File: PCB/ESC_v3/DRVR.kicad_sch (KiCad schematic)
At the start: 15 parts, among them U2 DRV8323SRTAT

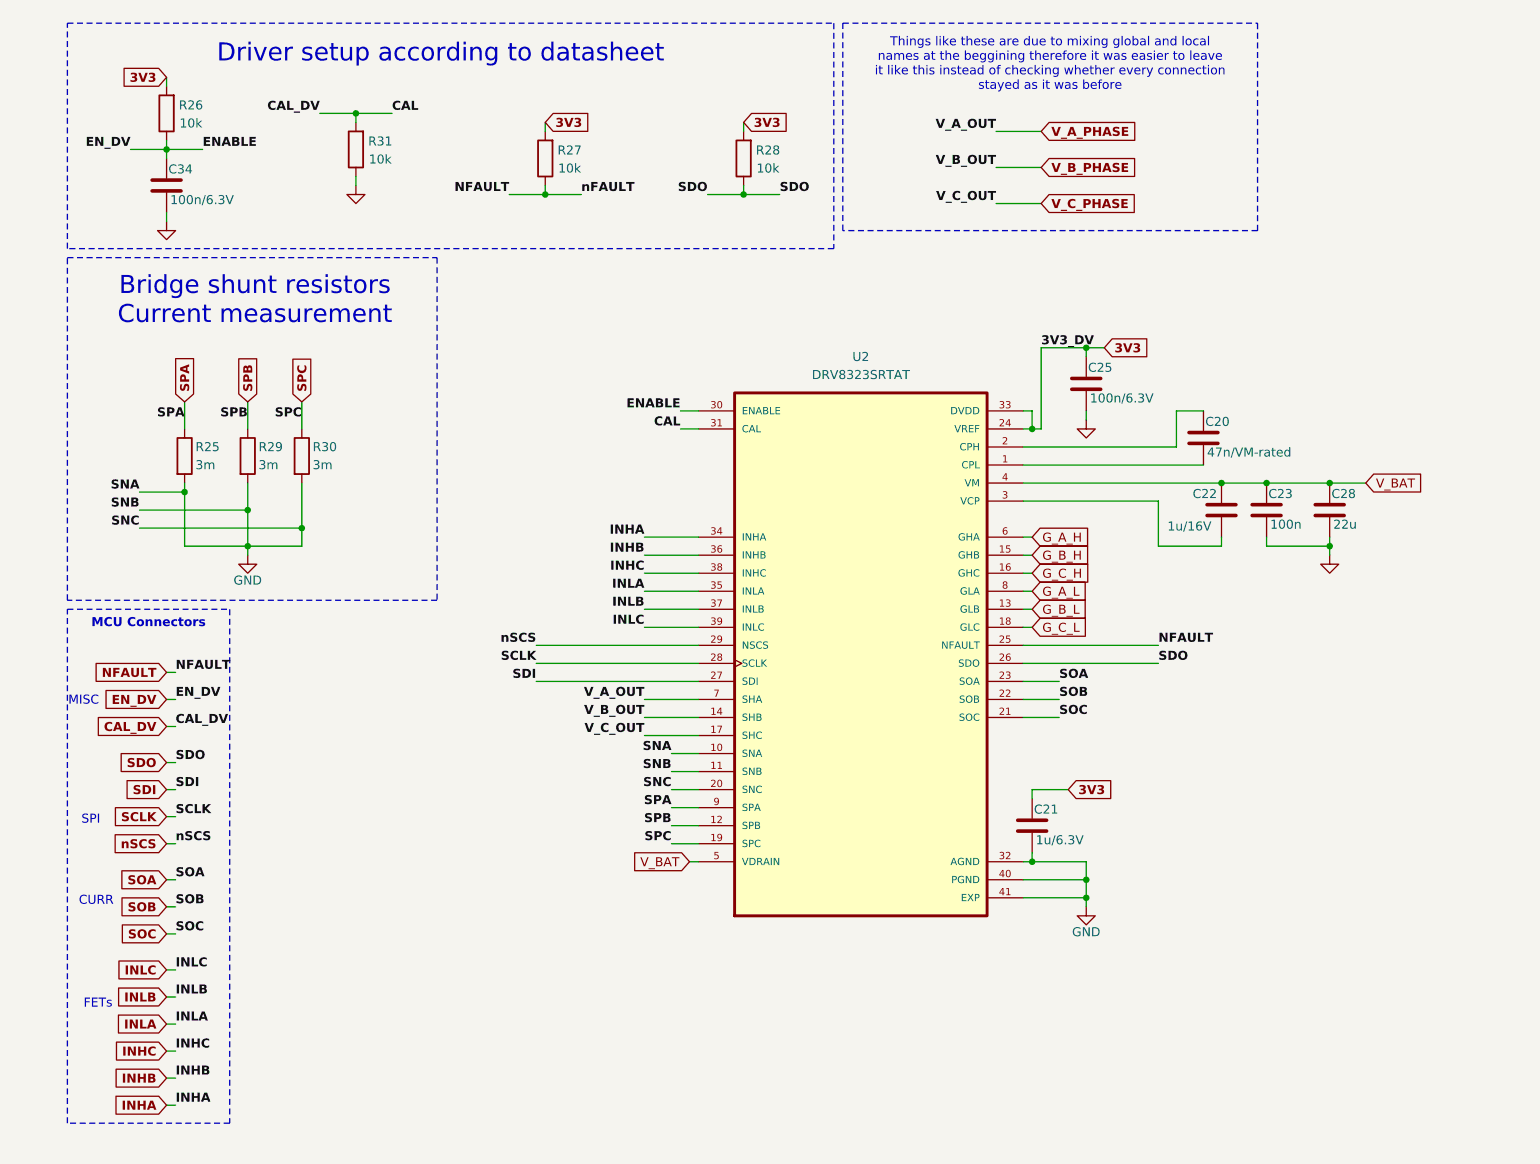
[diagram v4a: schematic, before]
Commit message: Update ESC_v3 schematics and PCB layout
Add net-tie symbol and +3V3/GND1 power symbols to DRVR schematic and reorganize schematic graphics (rectangles, text), junctions, and wires with updated coordinates/UUIDs. Also update top-level ESC_v3 schematic and MCU schematic along with PCB (.kicad_pcb) and panel (.kicad_prl) files. Remove several old backup zip files and add new backups for the ESC_v3 project.
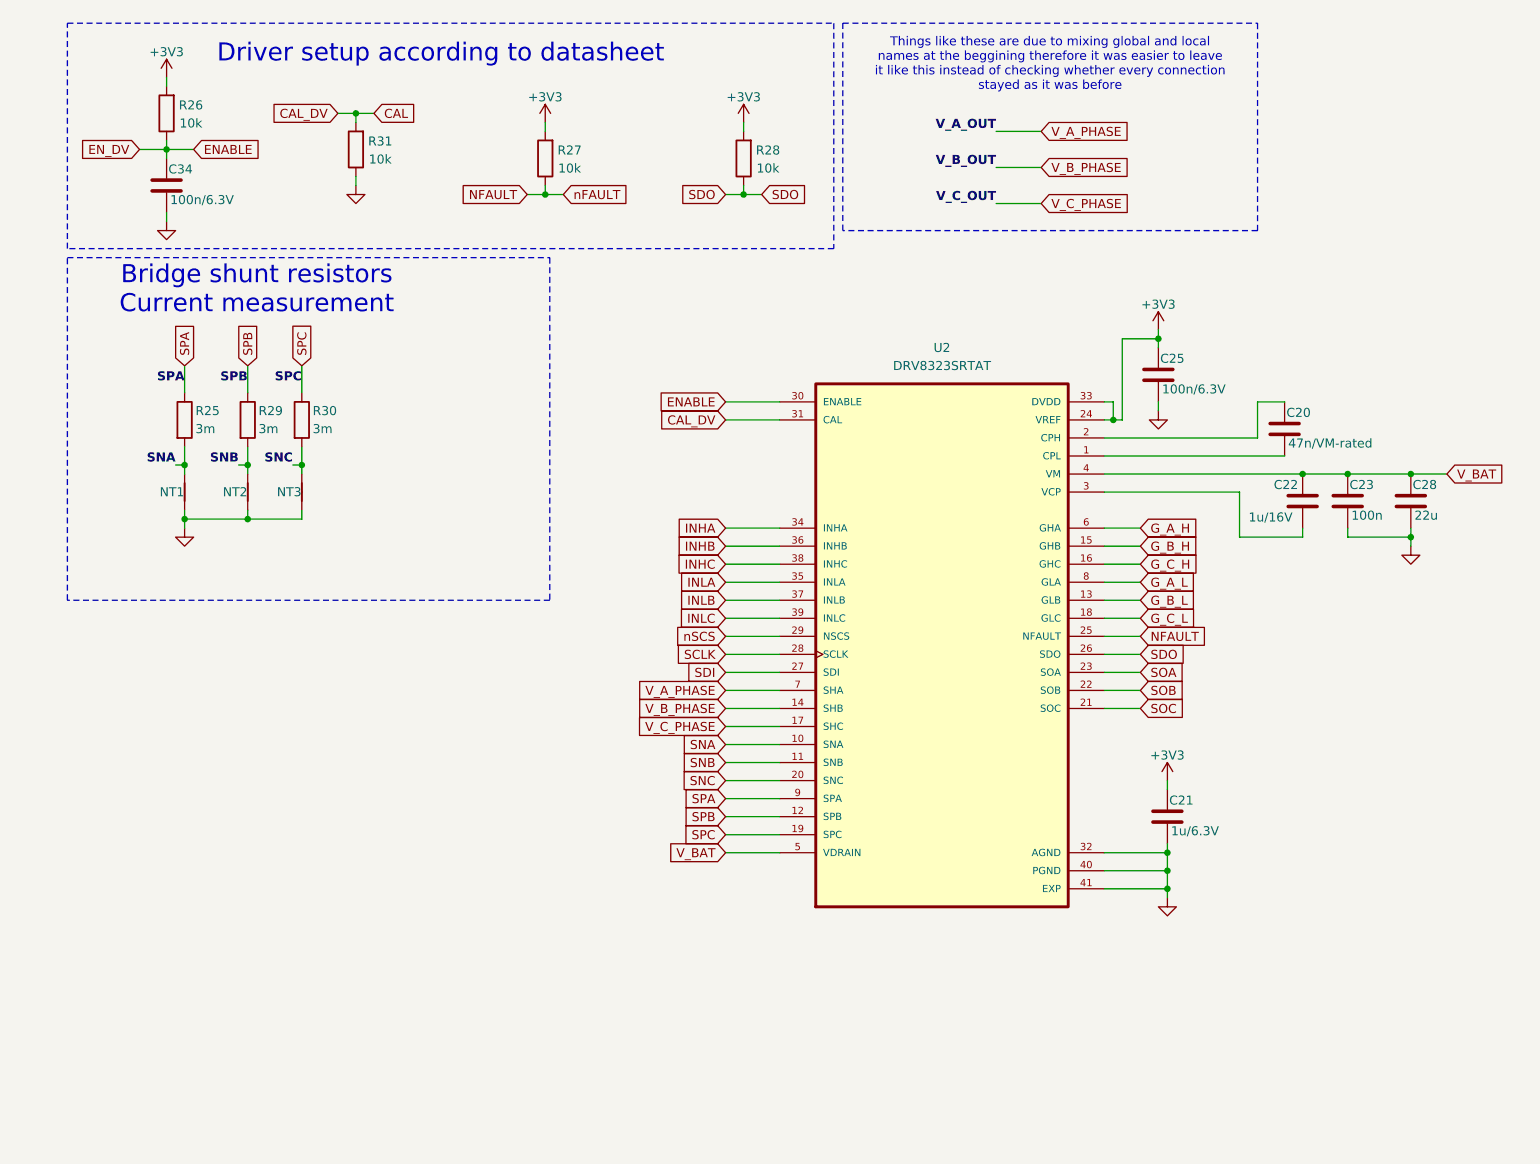
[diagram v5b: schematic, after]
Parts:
- added NT1, NT2, NT3: NetTie_2, symbol Device:NetTie_2
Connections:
- net GND: now also NT1.1, NT2.1, NT3.1; no longer R25.2, R29.2, R30.2, U2.10 (SNA), U2.11 (SNB), U2.20 (SNC)
- net 3V3 renamed +3V3
- net CAL_DV renamed CAL
- net EN_DV renamed ENABLE
- new net SNA: NT1.2, R25.2, U2.10 (SNA)
- new net SNB: NT2.2, R29.2, U2.11 (SNB)
- new net SNC: NT3.2, R30.2, U2.20 (SNC)
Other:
- note removed: "CURR"
- note removed: "FETs"
- note removed: "MCU Connectors"
- note removed: "MISC"
- note removed: "SPI"
- moved on the sheet: C20, C21, C22, C23, C25, C28, R25, R29, R30, U2

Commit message: Update DRVR schematic: relabels, wiring, net-ties
Refactor PCB/ESC_v3/DRVR.kicad_sch: cleaned up stray rectangles and comment text, repositioned many junctions and wires to fix connectivity, replaced/added global labels (reorganized SNA/SPA/SPB/SPC/SNB/SNC/etc.), and inserted NetTie symbols (NT1/NT3) with footprints to implement net ties. Updated symbol positions and UUIDs and removed obsolete schematic elements. Also touched top-level ESC_v3 files (ESC_v3.kicad_pcb, ESC_v3.kicad_prl, ESC_v3.kicad_sch, MCU.kicad_sch) and added/removed several backup archives.
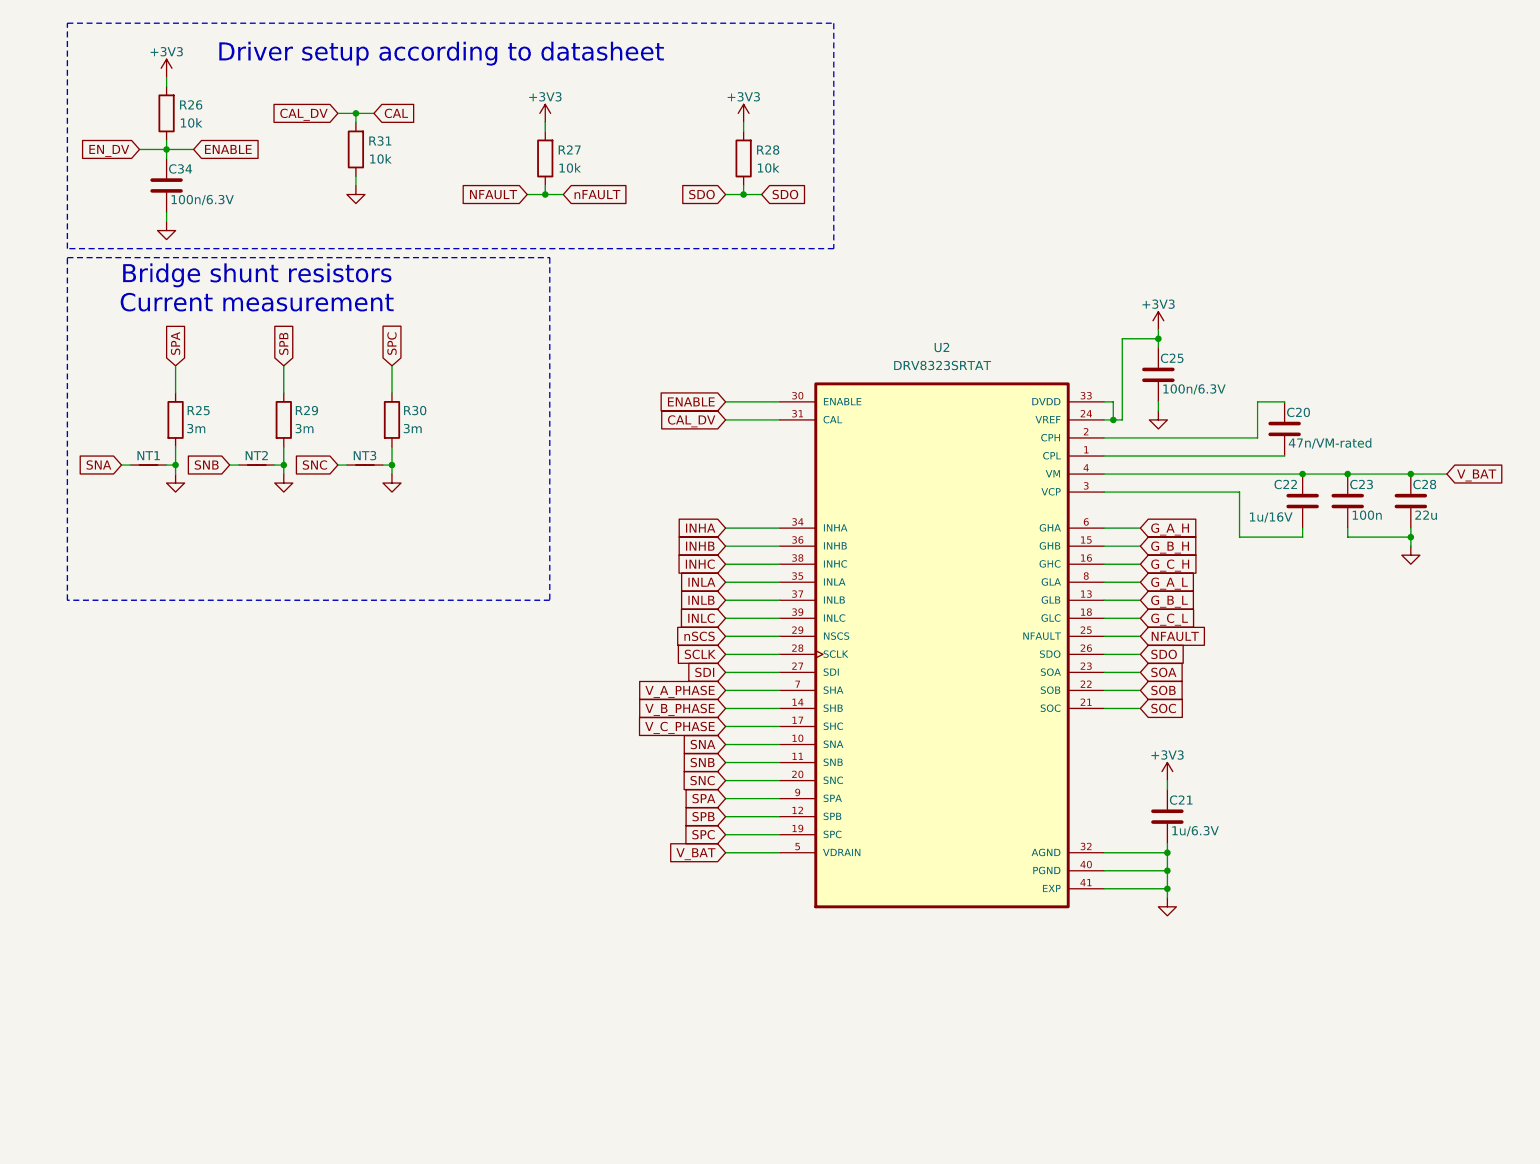
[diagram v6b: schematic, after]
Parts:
- NT1, NT2, NT3: footprint (none) -> NetTie:NetTie-2_SMD_Pad0.5mm
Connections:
- net GND: now also NT1.2, NT2.2, NT3.2, R25.2, R29.2, R30.2; no longer NT1.1, NT2.1, NT3.1
- net SNA: now also NT1.1; no longer NT1.2, R25.2
- net SNB: now also NT2.1; no longer NT2.2, R29.2
- net SNC: now also NT3.1; no longer NT3.2, R30.2
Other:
- note removed: "Things like these are due to mixing global and local names at the beggining therefore it was easier to leave it like this instead of checking whether every connection stayed as it was before"
- moved on the sheet: R25, R29, R30

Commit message: ESC_v3: footprint, PCB teardrops & backup updates
Remove Notes.txt; update ESC_v3 PCB and schematic files. In DRVR.kicad_sch several capacitor footprints changed from 0805 to 0603. ESC_v3.kicad_pcb: set grid_origin, added teardrops to multiple pads, updated many component UUIDs and silkscreen font thicknesses, and other layout metadata tweaks. Clean up old ESC_v3 backup zips and add new timestamped backup archives. Also update related KiCad project files (.kicad_prl, .kicad_pro). These changes shrink component footprints, improve manufacturability (teardrops), and refresh project backups/metadata.
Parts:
- C20, C22, C23: footprint Capacitor_SMD:C_0805_2012Metric -> Capacitor_SMD:C_0603_1608Metric
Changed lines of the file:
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@@
 			)
 		)
-		(property "Footprint" "Capacitor_SMD:C_0805_2012Metric"
+		(property "Footprint" "Capacitor_SMD:C_0603_1608Metric"
 			(at 191.4652 78.74 0)
 			(effects
@@
 			)
 		)
-		(property "Footprint" "Capacitor_SMD:C_0805_2012Metric"
+		(property "Footprint" "Capacitor_SMD:C_0603_1608Metric"
 			(at 200.3552 88.9 0)
 			(effects
@@
 			)
 		)
-		(property "Footprint" "Capacitor_SMD:C_0805_2012Metric"
+		(property "Footprint" "Capacitor_SMD:C_0603_1608Metric"
 			(at 194.0052 88.9 0)
 			(effects

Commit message: Layout edit
Changed some layout and optimized
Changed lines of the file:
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@@
-		)
-	)
-	(global_label "CAL_DV"
-		(shape input)
-		(at 111.76 73.66 180)
-		(fields_autoplaced yes)
-		(effects
-			(font
-				(size 1.27 1.27)
-				(thickness 0.1588)
-			)
-			(justify right)
-		)
-		(property "Intersheetrefs" "${INTERSHEET_REFS}"
-			(at 101.5859 73.66 0)
-			(effects
-				(font
-					(size 1.27 1.27)
-				)
-				(justify right)
-				(hide yes)
-			)
 		)
 	)
@@
 			(effects
 				(font
+					(size 1.27 1.27)
+				)
+				(justify right)
+				(hide yes)
+			)
+		)
+	)
+	(global_label "CAL"
+		(shape input)
+		(at 111.76 73.66 180)
+		(fields_autoplaced yes)
+		(effects
+			(font
+				(size 1.27 1.27)
+				(thickness 0.1588)
+			)
+			(justify right)
+		)
+		(property "Intersheetrefs" "${INTERSHEET_REFS}"
+			(at 105.3881 73.66 0)
+			(effects
+				(font
